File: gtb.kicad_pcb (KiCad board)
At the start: 2 copper layers, 44 x 50.8 mm, 10 parts, among them U1 7555

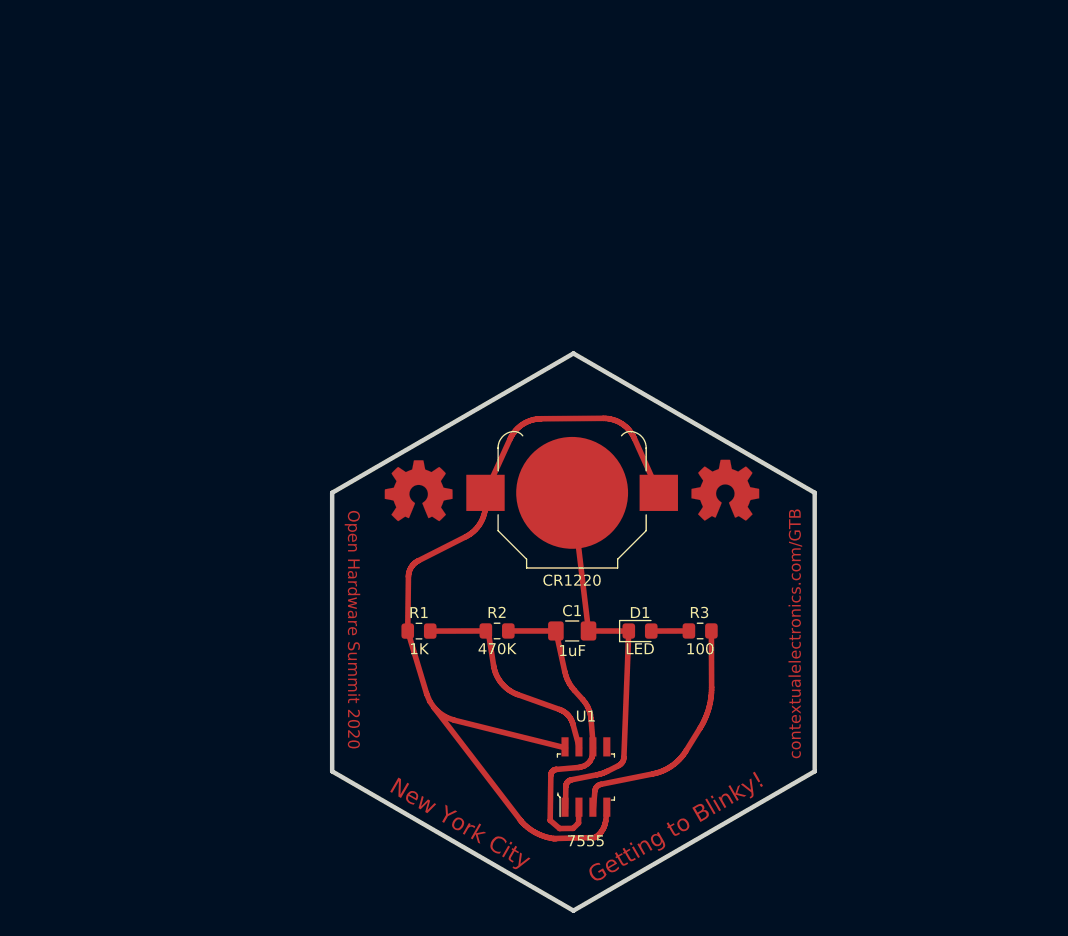
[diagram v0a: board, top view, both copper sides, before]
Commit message: flip to backside of board
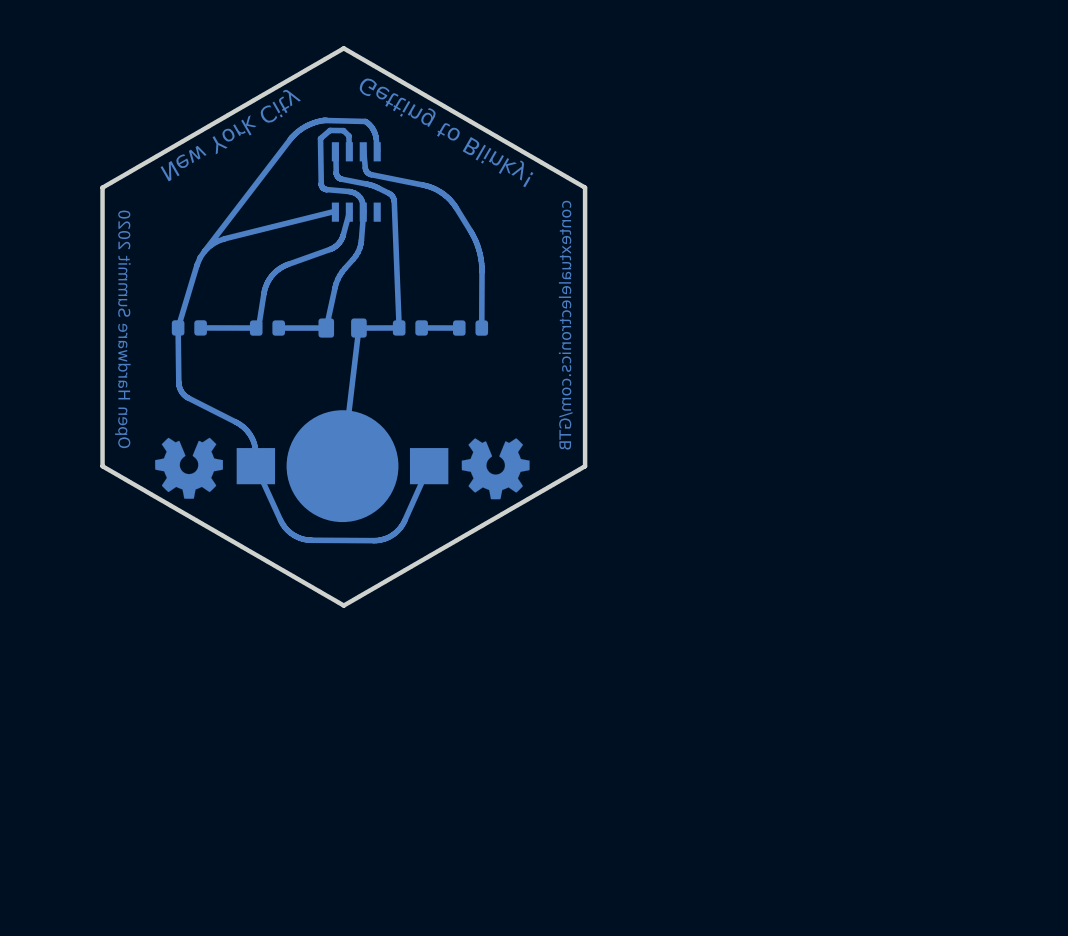
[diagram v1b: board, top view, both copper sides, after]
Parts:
- C1, CR1220, D1, R1, R2, R3, REF** (x3), U1: moved to B.Cu
- moved U1 58.2 mm to (157.6, 81.2)
- moved R1 34.7 mm to (142.4, 94.5)
- moved D1 34.7 mm to (162.5, 94.5)
- moved C1 34.7 mm to (156.4, 94.5)
- moved R2 34.7 mm to (149.5, 94.5)
- moved R3 34.7 mm to (168.0, 94.5)
- moved REF** 27.2 mm to (169.0, 99.6)
- moved REF** 21.3 mm to (142.4, 106.4)
- moved REF** 21.3 mm to (170.3, 106.4)
- moved CR1220 21.1 mm to (156.3, 107.1)

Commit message: update
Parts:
- removed the REF** at (170.3, 106.4)
- added D1: LED, LED_THT:LED_D3.0mm, F.Cu at (154.9, 82.8)
- added D1: LED, LED_THT:LED_D3.0mm, F.Cu at (155.1, 100.1)
- added D1: LED, LED_THT:LED_D3.0mm, F.Cu at (165.6, 95.1)
- C1: footprint Capacitor_SMD:C_1206_3216Metric_Pad1.42x1.75mm_HandSolder -> Capacitor_THT:C_Axial_L3.8mm_D2.6mm_P7.50mm_Horizontal; moved to F.Cu
- D1: footprint LED_SMD:LED_0805_2012Metric_Pad1.15x1.40mm_HandSolder -> LED_THT:LED_D3.0mm; moved to F.Cu
- R1, R2, R3: footprint Resistor_SMD:R_0805_2012Metric_Pad1.15x1.40mm_HandSolder -> Wickerlib:RES-CARBONFILM-7MM; moved to F.Cu
- U1: footprint digikey-footprints:SOIC-8-1EP_W3.9mm -> digikey-footprints:DIP-8_W7.62mm; moved to F.Cu
- moved REF** 81.1 mm to (217.4, 75.8), turned to 180 degrees
- moved REF** 50.0 mm to (216.5, 83.9), turned to 180 degrees
- moved C1 21.9 mm to (176.0, 104.3), turned to 90 degrees
- moved D1 17.6 mm to (144.9, 95.3), turned to 90 degrees
- moved R2 16.2 mm to (137.3, 105.2), turned to 90 degrees
- moved U1 15.1 mm to (152.1, 95.3), turned to 90 degrees
- moved R1 11.9 mm to (137.3, 83.7), turned to -90 degrees
- moved R3 8.05 mm to (175.9, 93.1), turned to 90 degrees
- moved CR1220 3.86 mm to (156.5, 111.0)
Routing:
- net /VDD: track 83.7 -> 0.00 mm
- net GND: track 36.2 -> 0.00 mm
- net Net-(C1-Pad1): track 29.8 -> 1.79 mm
- net Net-(R3-Pad1): track 22.6 -> 0.01 mm
- net Net-(R1-Pad2): track 19.8 -> 0.71 mm
- net Net-(D1-Pad2): track 3.43 -> 0.00 mm
- added copper zone on B.Cu, net /VDD
- added copper zone on F.Cu, net GND
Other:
- copper layers 2 -> 6
- net class Default removed
- net class ad removed
- board text removed: "Getting to Blinky!"
- board text removed: "New York City"
- board text removed: "Open Hardware Summit 2020"
